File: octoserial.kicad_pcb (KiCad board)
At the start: 2 copper layers, 110 x 82.5 mm, 49 parts, among them J1 USB_OTG, J10 Conn_01x03_Male, J3 Conn_01x03_Male, J4 Conn_01x03_Male, J5 Conn_01x03_Male, J6 Conn_01x03_Male, J7 Conn_01x03_Male, J8 Conn_01x03_Male, J9 Conn_01x03_Male, U1 AMS1117-3.3, U2 CH348Q, Y1 8MHz

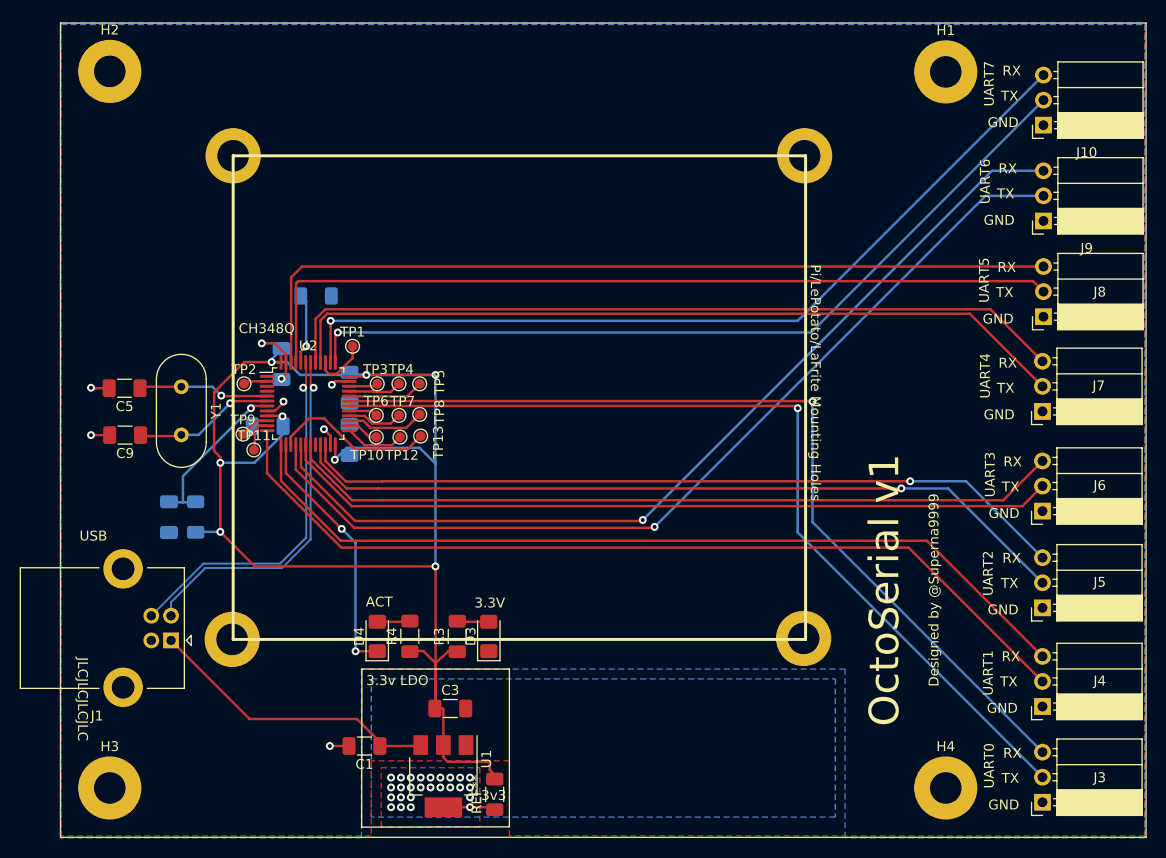
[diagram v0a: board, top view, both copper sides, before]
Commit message: Add gpio/3.3 headers
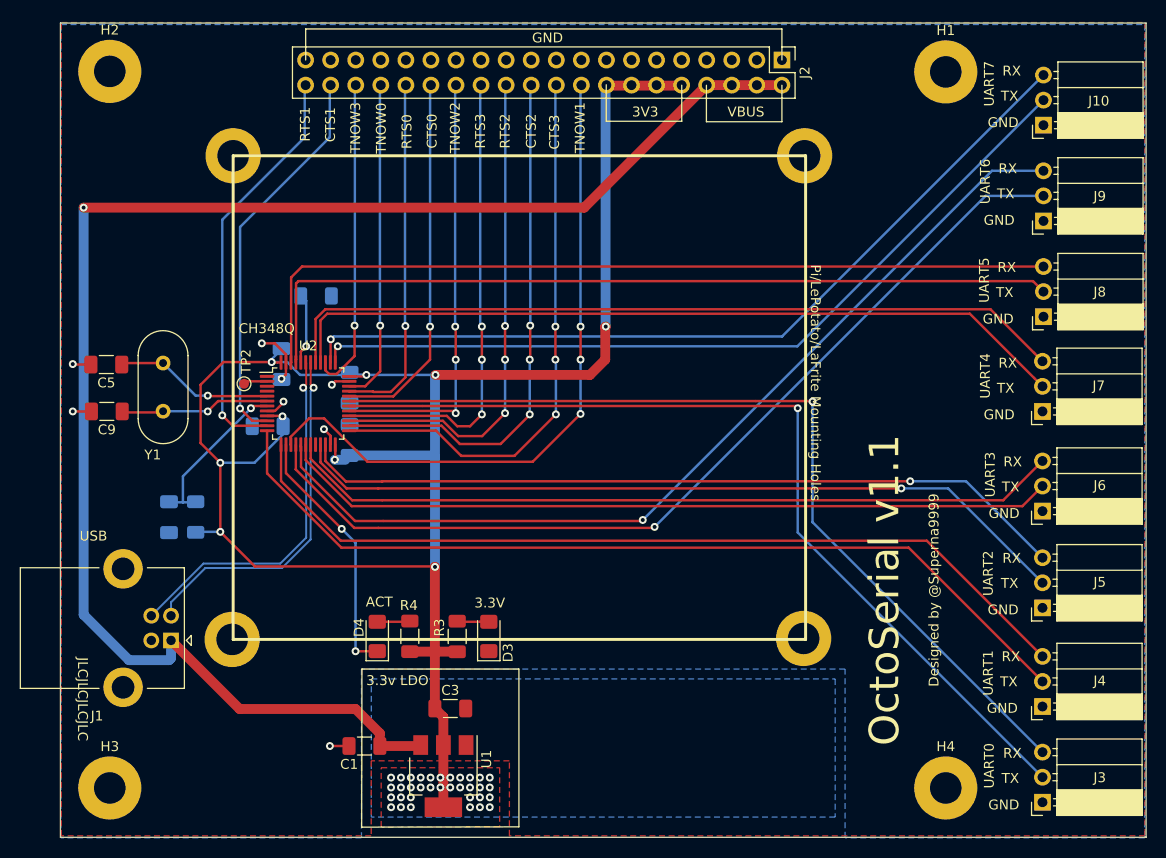
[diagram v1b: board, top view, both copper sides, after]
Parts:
- removed the REF** at (86.5, 114.7)
- removed TP1, TP10, TP11, TP12, TP13, TP3, TP4, TP5, TP6, TP7, TP8, TP9: TestPoint, TestPoint:TestPoint_Pad_D1.0mm
- added J2: Conn_02x20_Odd_Even, Connector_PinHeader_2.54mm:PinHeader_2x20_P2.54mm_Vertical, F.Cu at (115.6, 40.3)
- moved Y1 3.03 mm to (52.9, 71.0)
- moved C5 3.03 mm to (47.1, 71.2)
- moved C9 3.03 mm to (47.2, 75.9)
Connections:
- U2 pad 10: Net-(TP9-Pad1) -> /CTS1
- U2 pad 11: Net-(TP11-Pad1) -> /RTS1
- U2 pad 15: Net-(TP13-Pad1) -> /TNOW1
- U2 pad 25: Net-(TP12-Pad1) -> /CTS3
- U2 pad 26: Net-(TP10-Pad1) -> /CTS2
- U2 pad 27: Net-(TP8-Pad1) -> /RTS2
- U2 pad 28: Net-(TP7-Pad1) -> /RTS3
- U2 pad 29: Net-(TP6-Pad1) -> /TNOW2
- U2 pad 32: Net-(TP5-Pad1) -> /CTS0
- U2 pad 33: Net-(TP4-Pad1) -> /RTS0
- U2 pad 34: Net-(TP3-Pad1) -> /TNOW0
- U2 pad 39: Net-(TP1-Pad1) -> /TNOW3
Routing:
- net VBUS: track 30.2 -> 160.3 mm, vias 0 -> 1
- net /TNOW1: track 0.00 -> 68.0 mm, vias 0 -> 3
- net /CTS3: track 0.00 -> 57.1 mm, vias 0 -> 3
- net /CTS2: track 0.00 -> 53.6 mm, vias 0 -> 3
- net /RTS2: track 0.00 -> 50.6 mm, vias 0 -> 3
- net /RTS3: track 0.00 -> 47.5 mm, vias 0 -> 3
- net /TNOW2: track 0.00 -> 44.1 mm, vias 0 -> 3
- net /RTS1: track 0.00 -> 41.8 mm, vias 0 -> 1
- net /CTS1: track 0.00 -> 39.7 mm, vias 0 -> 1
- net /CTS0: track 0.00 -> 37.5 mm, vias 0 -> 1
- net /RTS0: track 0.00 -> 35.9 mm, vias 0 -> 1
- net +3V3: track 163.3 -> 197.8 mm, vias 34 -> 43
- net /TNOW0: track 0.00 -> 32.7 mm, vias 0 -> 1
- net /TNOW3: track 0.00 -> 32.1 mm, vias 0 -> 1
- net Net-(TP13-Pad1): track 16.6 -> 0.00 mm
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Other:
- board text added: "3V3"
- board text added: "CTS0"
- board text added: "CTS1"
- board text added: "CTS2"
- board text added: "CTS3"
- board text added: "OctoSerial v1.1"
- board text added: "RTS0"
- board text added: "RTS1"
- board text added: "RTS2"
- board text added: "RTS3"
- board text added: "TNOW0"
- board text added: "TNOW1"
- board text added: "TNOW2"
- board text added: "TNOW3"
- board text added: "VBUS"
- board text removed: "3v3"
- board text removed: "OctoSerial v1"

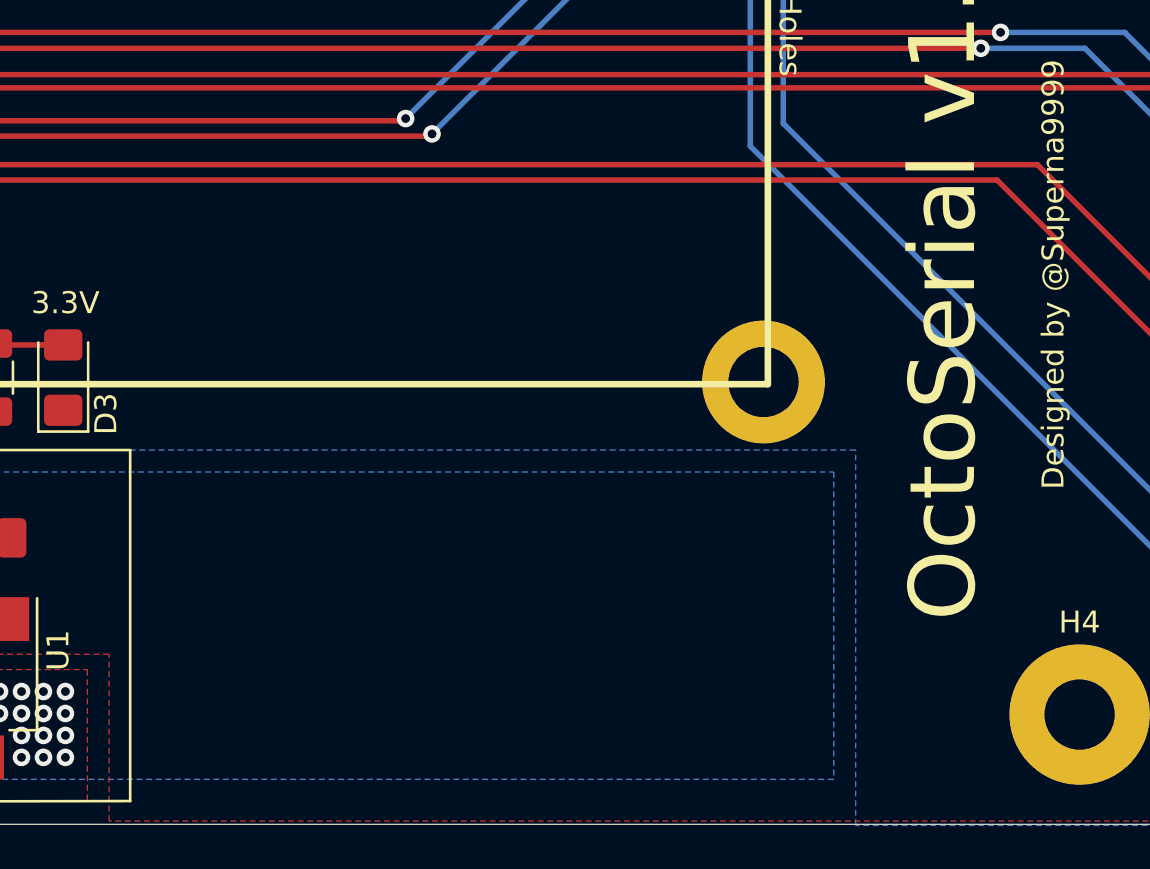
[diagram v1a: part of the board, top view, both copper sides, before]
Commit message: Add Kicad, OSHW + github URL on front silkscreen
Signed-off-by: Neil Armstrong <neil.armstrong@linaro.org>
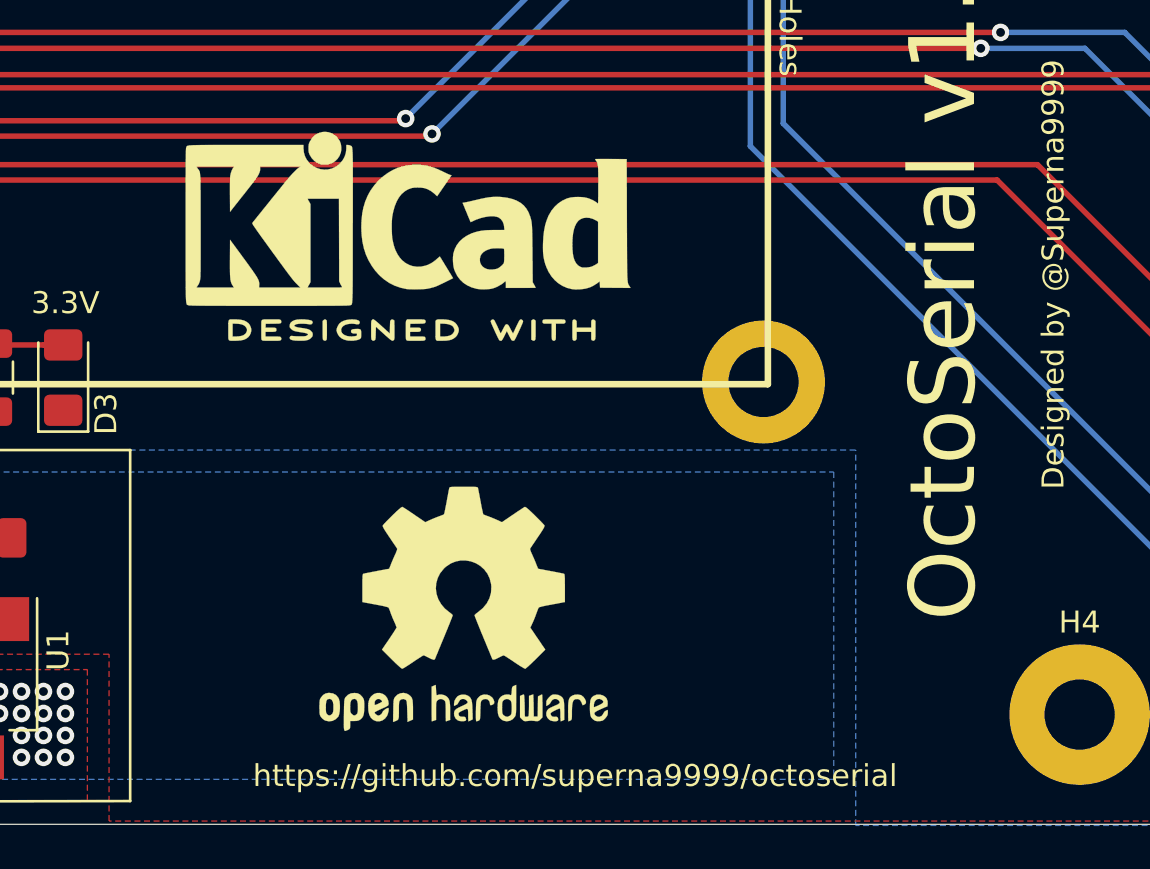
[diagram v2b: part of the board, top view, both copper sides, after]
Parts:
- added REF**: KiCad-Logo2_8mm_SilkScreen, Symbol:KiCad-Logo2_8mm_SilkScreen, F.Cu at (101.6, 91.4)
- added REF**: OSHW-Logo2_14.6x12mm_SilkScreen, Symbol:OSHW-Logo2_14.6x12mm_SilkScreen, F.Cu at (104.1, 109.2)
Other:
- board text added: "https://github.com/superna9999/octoserial"
